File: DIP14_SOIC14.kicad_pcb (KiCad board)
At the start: 2 copper layers, 8.9 x 16.5 mm, 3 parts

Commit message: kicad 6
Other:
- net class Default removed

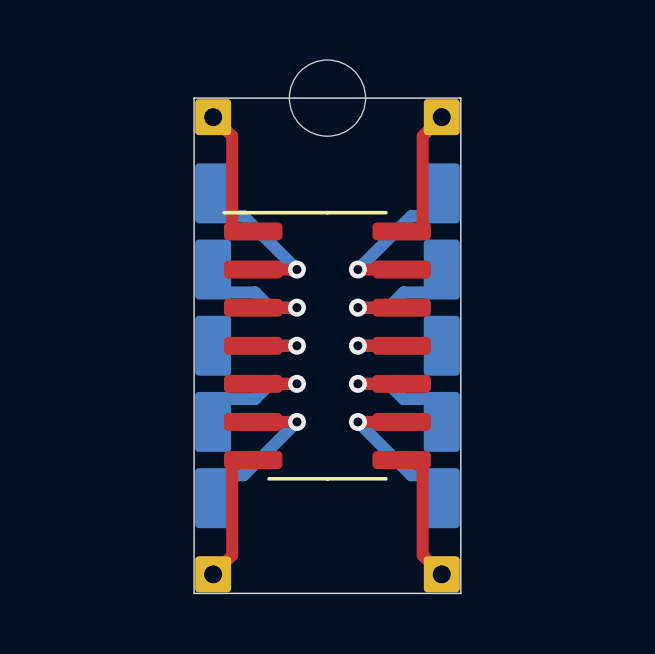
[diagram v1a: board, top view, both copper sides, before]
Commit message: Fix wrong pinout on FlashROM_100 TSOPgit add -A!
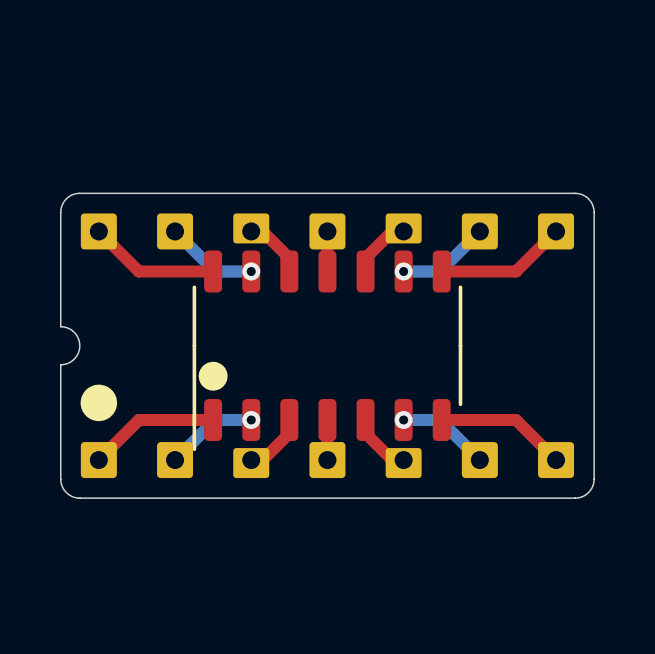
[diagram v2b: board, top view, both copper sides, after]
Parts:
- removed the REF** at (136.0, 95.6)
- turned REF** to 90 degrees (x2)
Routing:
- net (no net): track 71.5 -> 40.8 mm, vias 10 -> 4
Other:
- board size 8.9 x 16.5 mm -> 17.8 x 10.2 mm
- board text added: "${COMMENT2}"

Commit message: various minor cleanups
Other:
- outline, holes or cut-outs redrawn
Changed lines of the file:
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@@
   (title_block
     (title "SOIC14 to DIP14")
-    (date "2022-10-11")
-    (rev "002")
+    (date "2022-10-12")
+    (rev "003")
     (company "Bran. K. White - b.kenyon.w@gmail.com")
     (comment 2 "github.com/bkw777/aDIPters")
@@
   (gr_line (start 144.285 108.89) (end 127.775 108.89) (layer "Edge.Cuts") (width 0.05))
   (gr_line (start 144.92 108.255) (end 144.92 99.365) (layer "Edge.Cuts") (width 0.05))
-  (gr_line (start 127.14 108.255) (end 127.14 104.445) (layer "Edge.Cuts") (width 0.05))
+  (gr_line (start 127.14 108.255) (end 127.14 105.08) (layer "Edge.Cuts") (width 0.05))
   (gr_arc (start 144.285 98.73) (mid 144.734013 98.915987) (end 144.92 99.365) (layer "Edge.Cuts") (width 0.05))
-  (gr_arc (start 127.14 103.175) (mid 127.775 103.81) (end 127.14 104.445) (layer "Edge.Cuts") (width 0.05))
-  (gr_line (start 127.14 103.175) (end 127.14 99.365) (layer "Edge.Cuts") (width 0.05))
+  (gr_arc (start 127.14 102.54) (mid 128.41 103.81) (end 127.14 105.08) (layer "Edge.Cuts") (width 0.05))
+  (gr_line (start 127.14 102.54) (end 127.14 99.365) (layer "Edge.Cuts") (width 0.05))
   (gr_arc (start 144.92 108.255) (mid 144.734013 108.704013) (end 144.285 108.89) (layer "Edge.Cuts") (width 0.05))
   (gr_arc (start 127.14 99.365) (mid 127.325987 98.915987) (end 127.775 98.73) (layer "Edge.Cuts") (width 0.05))
   (gr_arc (start 127.775 108.89) (mid 127.325987 108.704013) (end 127.14 108.255) (layer "Edge.Cuts") (width 0.05))
-  (gr_text "${COMMENT2}" (at 136.03 105.08) (layer "B.SilkS")
+  (gr_text "${COMMENT2}" (at 136.03 101.905) (layer "B.SilkS")
     (effects (font (size 0.8 0.75) (thickness 0.1)) (justify mirror))
   )
